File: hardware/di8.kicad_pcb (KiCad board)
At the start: 2 copper layers, 88 parts, among them J101 TNG-Power-TOP, J102 TNG-Power-BTM, J103 TNG-Data-TOP, J104 TNG-Data-BTM, P101 BOOT, P201 INPUT0, P202 INPUT1, P203 INPUT2, P204 INPUT3, U101 STM32F070CBT6, U102 AP7333, U103 82400152, U201 ISO1212, U202 ISO1212, U203 ISO1212, U204 ISO1212, X101 TBD

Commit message: add first parts to pcb
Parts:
- D203, D204, D205, D206, D207, D208, D209, D210, J102, J104: moved to B.Cu
- moved J101 200.1 mm to (179.8, 127.5), turned to 270 degrees
- moved J102 195.8 mm to (179.8, 127.5), turned to 270 degrees
- moved J103 170.0 mm to (179.8, 82.5), turned to 270 degrees
- moved J104 167.4 mm to (179.8, 82.5), turned to 270 degrees
- moved P204 130.7 mm to (95.8, 137.5), turned to 270 degrees
- moved D210 119.8 mm to (101.4, 141.0), turned to 270 degrees
- moved P203 111.2 mm to (95.8, 121.5), turned to 270 degrees
- moved D209 109.6 mm to (101.4, 134.0), turned to 90 degrees
- moved D208 99.7 mm to (101.4, 125.0), turned to 90 degrees
- moved P202 95.8 mm to (95.8, 105.5), turned to 270 degrees
- moved D207 94.6 mm to (101.4, 118.0), turned to 90 degrees
- moved D206 87.2 mm to (101.4, 109.0), turned to 90 degrees
- moved D205 83.7 mm to (101.4, 102.0), turned to 270 degrees
- moved D204 82.0 mm to (101.4, 93.0), turned to 90 degrees
- moved P201 78.0 mm to (95.8, 89.5), turned to 270 degrees
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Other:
- board outline added: 100 x 85 mm

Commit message: partial placement
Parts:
- added R201: 1k, RMELF, F.Cu at (100.1, 91.2)
- added R202: 1k, RMELF, F.Cu at (100.1, 87.8)
- added R205: 1k, RMELF, F.Cu at (100.1, 107.2)
- added R206: 1k, RMELF, F.Cu at (100.1, 103.8)
- added R207: 1k, RMELF, F.Cu at (100.1, 123.2)
- added R208: 1k, RMELF, F.Cu at (100.1, 119.8)
- added R209: 1k, RMELF, F.Cu at (100.1, 139.2)
- added R210: 1k, RMELF, F.Cu at (100.1, 135.8)
- C202, C203, C205, C206, C207, C208, C209, C210: footprint C0603 -> C0805
- moved D216 123.3 mm to (103.3, 141.1), turned to 270 degrees
- moved D213 120.8 mm to (103.3, 133.9), turned to 90 degrees
- moved C209 117.5 mm to (105.0, 139.7), turned to 270 degrees
- moved R215 113.5 mm to (106.5, 139.8), turned to 270 degrees
- moved C210 112.7 mm to (105.0, 135.6), turned to 270 degrees
- moved U204 112.2 mm to (110.8, 137.5), turned to 90 degrees
- moved D212 111.9 mm to (103.3, 117.9), turned to 90 degrees
- moved R216 111.1 mm to (106.5, 135.8), turned to 270 degrees
- moved D215 109.8 mm to (103.3, 125.1), turned to 270 degrees
- moved D214 107.8 mm to (103.3, 109.1), turned to 270 degrees
- moved D211 99.9 mm to (103.3, 101.9), turned to 90 degrees
- moved D201 91.6 mm to (103.3, 85.9), turned to 90 degrees
- moved D202 90.6 mm to (103.3, 93.1), turned to 270 degrees
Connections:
- P201 pad 2: (no net) -> Net-(P201-Pad2)
- P201 pad 3: (no net) -> Net-(P201-Pad3)
- P202 pad 2: (no net) -> Net-(P202-Pad2)
- P202 pad 3: (no net) -> Net-(P202-Pad3)
- P203 pad 2: (no net) -> Net-(P203-Pad2)
- P203 pad 3: (no net) -> Net-(P203-Pad3)
- P204 pad 2: (no net) -> Net-(P204-Pad2)
- P204 pad 3: (no net) -> Net-(P204-Pad3)
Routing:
- net AGND: track 0.00 -> 8.25 mm
- net Net-(C209-Pad2): track 0.00 -> 7.76 mm
- net Net-(C210-Pad2): track 0.00 -> 7.08 mm
- net Net-(P204-Pad3): track 0.00 -> 2.85 mm
- net Net-(P204-Pad2): track 0.00 -> 2.85 mm
- net Net-(R216-Pad1): track 0.00 -> 2.14 mm
- net Net-(R215-Pad1): track 0.00 -> 1.77 mm

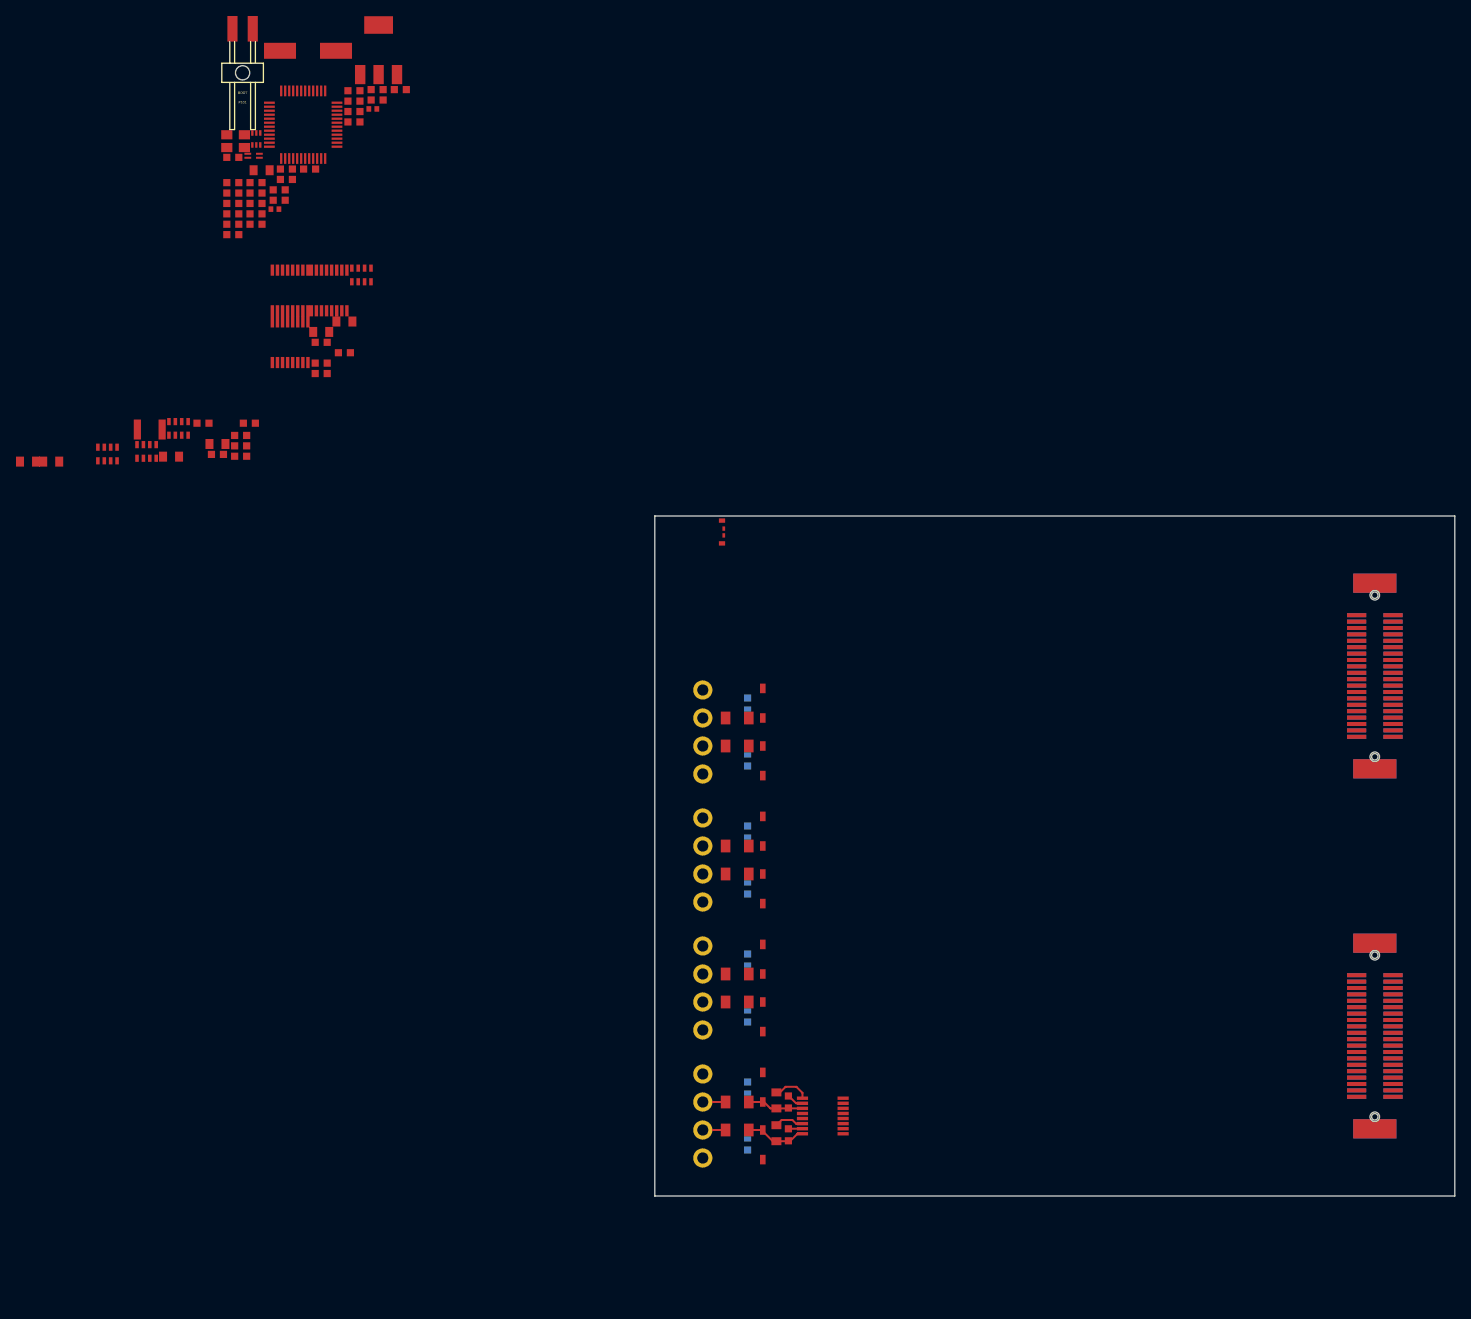
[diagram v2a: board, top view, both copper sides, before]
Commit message: add dc dc converter, routing
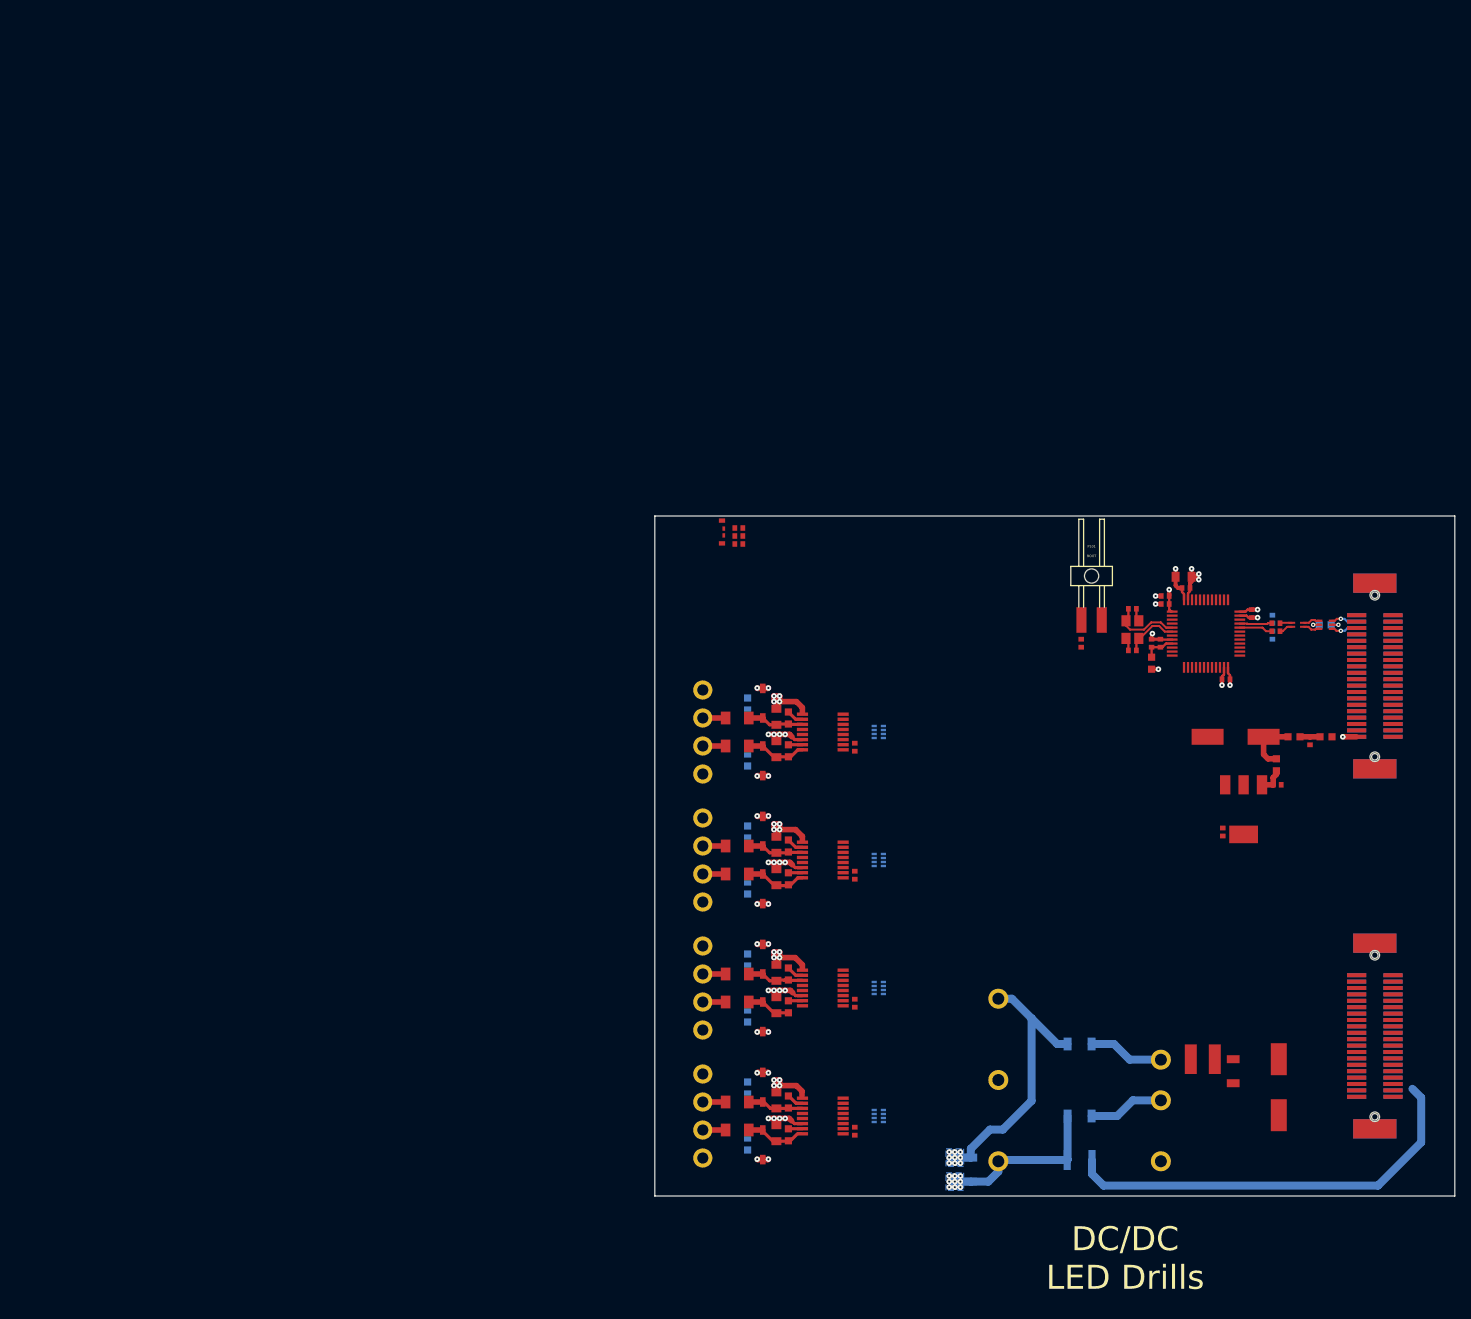
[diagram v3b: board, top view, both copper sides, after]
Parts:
- removed R107: TBD, R0603F
- added C118: 10µF/35V, C1206, B.Cu at (129.3, 144.2)
- added C119: 1nF 2kV, C1206, B.Cu at (142.9, 128.5)
- added C120: 1nF 2kV, C1206, B.Cu at (142.9, 137.5)
- added C121: 10µF/35V, C1206, F.Cu at (162.1, 131.9)
- added C122: 100µF/35V, kicad-libraries:ELKO_83, F.Cu at (167.8, 133.9)
- added L106: 4.7uH, kicad-libraries:NR4040, F.Cu at (158.3, 130.4)
- added U104: PDQE10, kicad-libraries:PDQE10, F.Cu at (142.9, 133.0)
- C101, C102, C103, C104, C105, C106, C107, C108, C109, C112, C204, C211, C212, C213: footprint C0603F -> C0402F
- C113, C114: footprint C0603F -> C0402F; moved to B.Cu
- C115, C201: moved to B.Cu
- R101, R103, R104: footprint R0603F -> R0402F
- R102, R105: value TBD -> 0; footprint R0603F -> R0402F
- R106: value TBD -> 56; footprint R0603F -> R0402F
- RP201, RP202, RP203, RP204: footprint 4X0603 -> kicad-libraries:4X0402; moved to B.Cu
- moved L104 151.5 mm to (173.7, 90.1), turned to 180 degrees
- moved C112 147.9 mm to (171.7, 90.6), turned to 270 degrees
- moved C201 147.8 mm to (142.9, 143.0), turned to 180 degrees
- moved U103 146.8 mm to (173.7, 76.1), turned to 270 degrees
- moved L102 144.3 mm to (167.5, 93.6), turned to 270 degrees
- moved C111 144.2 mm to (162.4, 90.1)
- moved U102 143.9 mm to (163.4, 99.2), turned to 180 degrees
- moved L105 143.1 mm to (170.2, 76.1), turned to 180 degrees
- moved C116 141.8 mm to (160.8, 102.0), turned to 90 degrees
- moved C117 141.1 mm to (167.6, 96.1)
- moved C114 139.3 mm to (167.0, 77.4), turned to 270 degrees
- moved C113 139.0 mm to (167.0, 75.4), turned to 90 degrees
- moved C103 138.2 mm to (161.2, 82.9), turned to 180 degrees
- moved L103 137.9 mm to (169.7, 90.1), turned to 180 degrees
- moved C104 137.3 mm to (164.4, 74.7), turned to 270 degrees
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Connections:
- J101 pad 1: AGND -> Net-(C120-Pad2)
- J101 pad 10: VCC -> Net-(C121-Pad1)
- J101 pad 11: AGND -> Net-(C120-Pad2)
- J101 pad 12: VCC -> Net-(C121-Pad1)
- J101 pad 13: AGND -> Net-(C120-Pad2)
- J101 pad 14: VCC -> Net-(C121-Pad1)
- J101 pad 15: AGND -> Net-(C120-Pad2)
- J101 pad 16: VCC -> Net-(C121-Pad1)
- J101 pad 17: AGND -> Net-(C120-Pad2)
- J101 pad 18: VCC -> Net-(C121-Pad1)
- J101 pad 19: AGND -> Net-(C120-Pad2)
- J101 pad 2: VCC -> Net-(C121-Pad1)
- J101 pad 20: VCC -> Net-(C121-Pad1)
- J101 pad 3: AGND -> Net-(C120-Pad2)
- J101 pad 4: VCC -> Net-(C121-Pad1)
- J101 pad 5: AGND -> Net-(C120-Pad2)
- J101 pad 6: VCC -> Net-(C121-Pad1)
- J101 pad 7: AGND -> Net-(C120-Pad2)
- J101 pad 8: VCC -> Net-(C121-Pad1)
- J101 pad 9: AGND -> Net-(C120-Pad2)
- J102 pad 1: VCC -> Net-(C121-Pad1)
- J102 pad 10: AGND -> Net-(C120-Pad2)
- J102 pad 11: VCC -> Net-(C121-Pad1)
- J102 pad 12: AGND -> Net-(C120-Pad2)
- J102 pad 13: VCC -> Net-(C121-Pad1)
- J102 pad 14: AGND -> Net-(C120-Pad2)
- J102 pad 15: VCC -> Net-(C121-Pad1)
- J102 pad 16: AGND -> Net-(C120-Pad2)
- J102 pad 17: VCC -> Net-(C121-Pad1)
- J102 pad 18: AGND -> Net-(C120-Pad2)
- J102 pad 19: VCC -> Net-(C121-Pad1)
- J102 pad 2: AGND -> Net-(C120-Pad2)
- J102 pad 20: AGND -> Net-(C120-Pad2)
- J102 pad 3: VCC -> Net-(C121-Pad1)
- J102 pad 4: AGND -> Net-(C120-Pad2)
- J102 pad 5: VCC -> Net-(C121-Pad1)
- J102 pad 6: AGND -> Net-(C120-Pad2)
- J102 pad 7: VCC -> Net-(C121-Pad1)
- J102 pad 8: AGND -> Net-(C120-Pad2)
- J102 pad 9: VCC -> Net-(C121-Pad1)
- LED101 pad 1: Net-(LED101-Pad1) -> 3V3
- R106 pad 1: LEDR -> LEDB
- RP201 pad 1: Net-(D203-Pad2) -> LED0
- RP201 pad 2: Net-(D203-Pad1) -> 3V3
- RP201 pad 3: Net-(D204-Pad2) -> LED1
- RP201 pad 4: Net-(D204-Pad1) -> 3V3
- RP201 pad 5: 3V3 -> Net-(D204-Pad1)
- RP201 pad 6: (no net) -> Net-(D204-Pad2)
- RP201 pad 7: 3V3 -> Net-(D203-Pad1)
- RP201 pad 8: LED0 -> Net-(D203-Pad2)
- RP202 pad 1: Net-(D205-Pad2) -> LED2
- RP202 pad 2: Net-(D205-Pad1) -> 3V3
- RP202 pad 3: Net-(D206-Pad2) -> LED3
- RP202 pad 4: Net-(D206-Pad1) -> 3V3
- RP202 pad 5: 3V3 -> Net-(D206-Pad1)
- RP202 pad 6: LED3 -> Net-(D206-Pad2)
- RP202 pad 7: 3V3 -> Net-(D205-Pad1)
- RP202 pad 8: LED2 -> Net-(D205-Pad2)
- RP203 pad 1: Net-(D207-Pad2) -> LED4
- RP203 pad 2: Net-(D207-Pad1) -> 3V3
- RP203 pad 3: Net-(D208-Pad2) -> LED5
- RP203 pad 4: Net-(D208-Pad1) -> 3V3
- RP203 pad 5: 3V3 -> Net-(D208-Pad1)
- RP203 pad 6: LED5 -> Net-(D208-Pad2)
- RP203 pad 7: 3V3 -> Net-(D207-Pad1)
- RP203 pad 8: LED4 -> Net-(D207-Pad2)
- RP204 pad 1: Net-(D209-Pad2) -> LED6
- RP204 pad 2: Net-(D209-Pad1) -> 3V3
- RP204 pad 3: Net-(D210-Pad2) -> LED7
- RP204 pad 4: Net-(D210-Pad1) -> 3V3
- RP204 pad 5: 3V3 -> Net-(D210-Pad1)
- RP204 pad 6: LED7 -> Net-(D210-Pad2)
- RP204 pad 7: 3V3 -> Net-(D209-Pad1)
- RP204 pad 8: LED6 -> Net-(D209-Pad2)
- U101 pad 12: LED2 -> LED0
- U101 pad 13: LED3 -> LED1
- U101 pad 14: (no net) -> LED2
- U101 pad 15: LED4 -> LED3
- U101 pad 16: (no net) -> LED4
- U101 pad 18: (no net) -> IN0
- U101 pad 19: (no net) -> IN1
- U101 pad 20: LED0 -> IN2
- U101 pad 27: LEDG -> (no net)
- U101 pad 28: LEDR -> (no net)
- U101 pad 29: (no net) -> LEDR
- U101 pad 30: (no net) -> LEDG
- U101 pad 31: (no net) -> LEDB
- U101 pad 39: (no net) -> IN3
- U101 pad 40: (no net) -> IN4
- U101 pad 41: (no net) -> IN4
- U101 pad 42: (no net) -> IN6
- U101 pad 43: (no net) -> IN7
- U101 pad 46: LEDR -> (no net)
- U201 pad 4: (no net) -> IN0
- U201 pad 5: (no net) -> IN1
- U202 pad 4: (no net) -> IN2
- U202 pad 5: (no net) -> IN3
- U203 pad 4: (no net) -> IN4
- U204 pad 4: (no net) -> IN6
- U204 pad 5: (no net) -> IN7
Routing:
- net AGND: track 8.25 -> 120.6 mm, vias 0 -> 57
- net Earth: track 0.00 -> 52.9 mm
- net VCC: track 0.00 -> 39.4 mm, vias 0 -> 9
- net GND: track 0.00 -> 19.6 mm, vias 0 -> 9
- net 3V3: track 0.00 -> 13.1 mm, vias 0 -> 5
- net Net-(C120-Pad2): track 0.00 -> 9.47 mm
- net Net-(C119-Pad2): track 0.00 -> 9.47 mm
- net Net-(C108-Pad2): track 0.00 -> 8.85 mm
- net Net-(C208-Pad2): track 0.00 -> 8.03 mm
- net Net-(C205-Pad2): track 0.00 -> 7.72 mm
- net Net-(C202-Pad2): track 0.00 -> 7.72 mm
- net Net-(C206-Pad2): track 0.00 -> 7.12 mm
- net Net-(C203-Pad2): track 0.00 -> 7.12 mm
- net +5V: track 0.00 -> 7.08 mm
- net Net-(C109-Pad2): track 0.00 -> 6.73 mm
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- added copper zone on B.Cu, net AGND
- added copper zone on GND, net AGND
- added copper zone on B.Cu, net VCC
- added copper zone on VCC, net VCC
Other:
- copper layers 2 -> 4
- net class DIFF_90 added: clearance 0.15, trace_width 0.25, via_dia 0.55, via_drill 0.25
- net class Default: clearance 0.2 -> 0.15; trace_width 0.25 -> 0.15; via_dia 0.8 -> 0.55; via_drill 0.4 -> 0.25
- rule trace_clearance: 0.2 -> 0.15
- rule trace_min: 0.2 -> 0.15
- rule via_min_drill: 0.3 -> 0.25
- board text added: "DC/DC LED Drills"

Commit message: more routing
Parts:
- turned D203 to 90 degrees
- turned D205 to 90 degrees
- turned D210 to 90 degrees
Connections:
- U101 pad 34: LED5 -> LED7
- U101 pad 38: LED7 -> LED5
- U101 pad 41: IN4 -> IN5
- U203 pad 5: (no net) -> IN5
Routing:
- net IN6: track 0.00 -> 95.1 mm, vias 0 -> 2
- net IN7: track 0.00 -> 94.1 mm, vias 0 -> 2
- net LED6: track 0.00 -> 87.9 mm, vias 0 -> 1
- net LED7: track 0.00 -> 87.8 mm, vias 0 -> 1
- net IN4: track 0.00 -> 86.8 mm, vias 0 -> 2
- net IN5: track 0.00 -> 79.1 mm, vias 0 -> 2
- net LEDG: track 0.00 -> 74.0 mm, vias 0 -> 2
- net LEDB: track 0.00 -> 73.2 mm, vias 0 -> 2
- net LEDR: track 0.00 -> 72.6 mm, vias 0 -> 2
- net LED5: track 0.00 -> 71.4 mm, vias 0 -> 1
- net IN3: track 0.00 -> 64.7 mm, vias 0 -> 2
- net LED4: track 0.00 -> 60.3 mm, vias 0 -> 1
- net IN2: track 0.00 -> 58.2 mm
- net IN1: track 0.00 -> 50.4 mm, vias 0 -> 2
- net IN0: track 0.00 -> 49.9 mm
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- added copper zone on VCC, net 3V3
- added copper zone on GND, net GND

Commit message: routing completed
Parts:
- added G***: LOGO, kicad-libraries:Logo_TF_10x12, F.Cu at (102.6, 74.6)
- added P102: Debug, kicad-libraries:DEBUG_PAD, F.Cu at (164.8, 80.2)
- added R107: 1k, R0402F, B.Cu at (172.9, 74.1)
- added R108: 1k, R0402F, B.Cu at (171.0, 74.1)
- D203, D204, D205, D206, D207, D208, D209, D210: footprint D0603F -> LED-LP
- LED101: footprint EASV3015RGBA0 -> LED-RGB-LP
- U104: footprint kicad-libraries:PDQE10 -> PDQE10
- moved C113 1.00 mm to (166.0, 75.4)
- moved C114 1.00 mm to (166.0, 77.4)
- moved C115 1.00 mm to (172.6, 76.1)
- moved L105 1.00 mm to (169.2, 76.1)
- moved R103 1.00 mm to (166.4, 75.9)
- moved R104 1.00 mm to (166.4, 76.9)
- moved U103 1.00 mm to (172.7, 76.1)
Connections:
- net Net-(C120-Pad2) renamed AGNDA
- net Net-(C121-Pad1) renamed VCCPWRA
- net Net-(J104-Pad4) renamed USB-DPA
- net Net-(J104-Pad6) renamed USB-DMA
- net Net-(L105-Pad1) renamed USB-DMB
- net Net-(L105-Pad2) renamed USB-DMC
- net Net-(L105-Pad3) renamed USB-DPC
- net Net-(L105-Pad4) renamed USB-DPB
- U101 pad 10: (no net) -> AIN0
- U101 pad 25: (no net) -> Net-(P102-Pad1)
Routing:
- net GND: track 37.7 -> 129.7 mm, vias 22 -> 66
- net 5VA: track 3.47 -> 56.6 mm, vias 2 -> 12
- net VCCPWRA: track 8.00 -> 46.3 mm, vias 0 -> 15
- net AGNDA: track 26.8 -> 63.5 mm, vias 0 -> 15
- net Earth: track 52.9 -> 86.3 mm, vias 0 -> 10
- net AIN0: track 0.00 -> 28.7 mm, vias 0 -> 1
- net 3V3: track 39.7 -> 56.7 mm, vias 16 -> 21
- net Net-(J103-Pad19): track 0.00 -> 10.9 mm, vias 0 -> 1
- net Net-(J103-Pad27): track 0.00 -> 9.15 mm, vias 0 -> 1
- net Net-(J103-Pad3): track 0.00 -> 7.85 mm, vias 0 -> 1
- net Net-(J103-Pad11): track 0.00 -> 7.85 mm, vias 0 -> 1
- net Net-(J103-Pad5): track 0.00 -> 7.71 mm, vias 0 -> 1
- net Net-(J103-Pad13): track 0.00 -> 7.71 mm, vias 0 -> 1
- net Net-(J103-Pad21): track 0.00 -> 7.71 mm, vias 0 -> 1
- net Net-(J103-Pad29): track 0.00 -> 6.36 mm, vias 0 -> 1
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- added copper zone on F.Cu, net 5VA
- added copper zone on GND, net AGNDA
- added copper zone on B.Cu, net Earth
- added copper zone on VCC, net VCCPWRA
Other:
- board text added: "DI 0"
- board text added: "DI 1"
- board text added: "DI 2"
- board text added: "DI 3"
- board text added: "DI 4"
- board text added: "DI 5"
- board text added: "DI 6"
- board text added: "DI 7"
- board text added: "DI8 1.0"
- board text added: "GND"
- board text added: "GND 3.3V 5V"
- board text added: "VCC"
- board text removed: "DC/DC LED Drills"
